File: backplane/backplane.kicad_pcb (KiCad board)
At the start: 2 copper layers, 150 x 150 mm, 14 parts

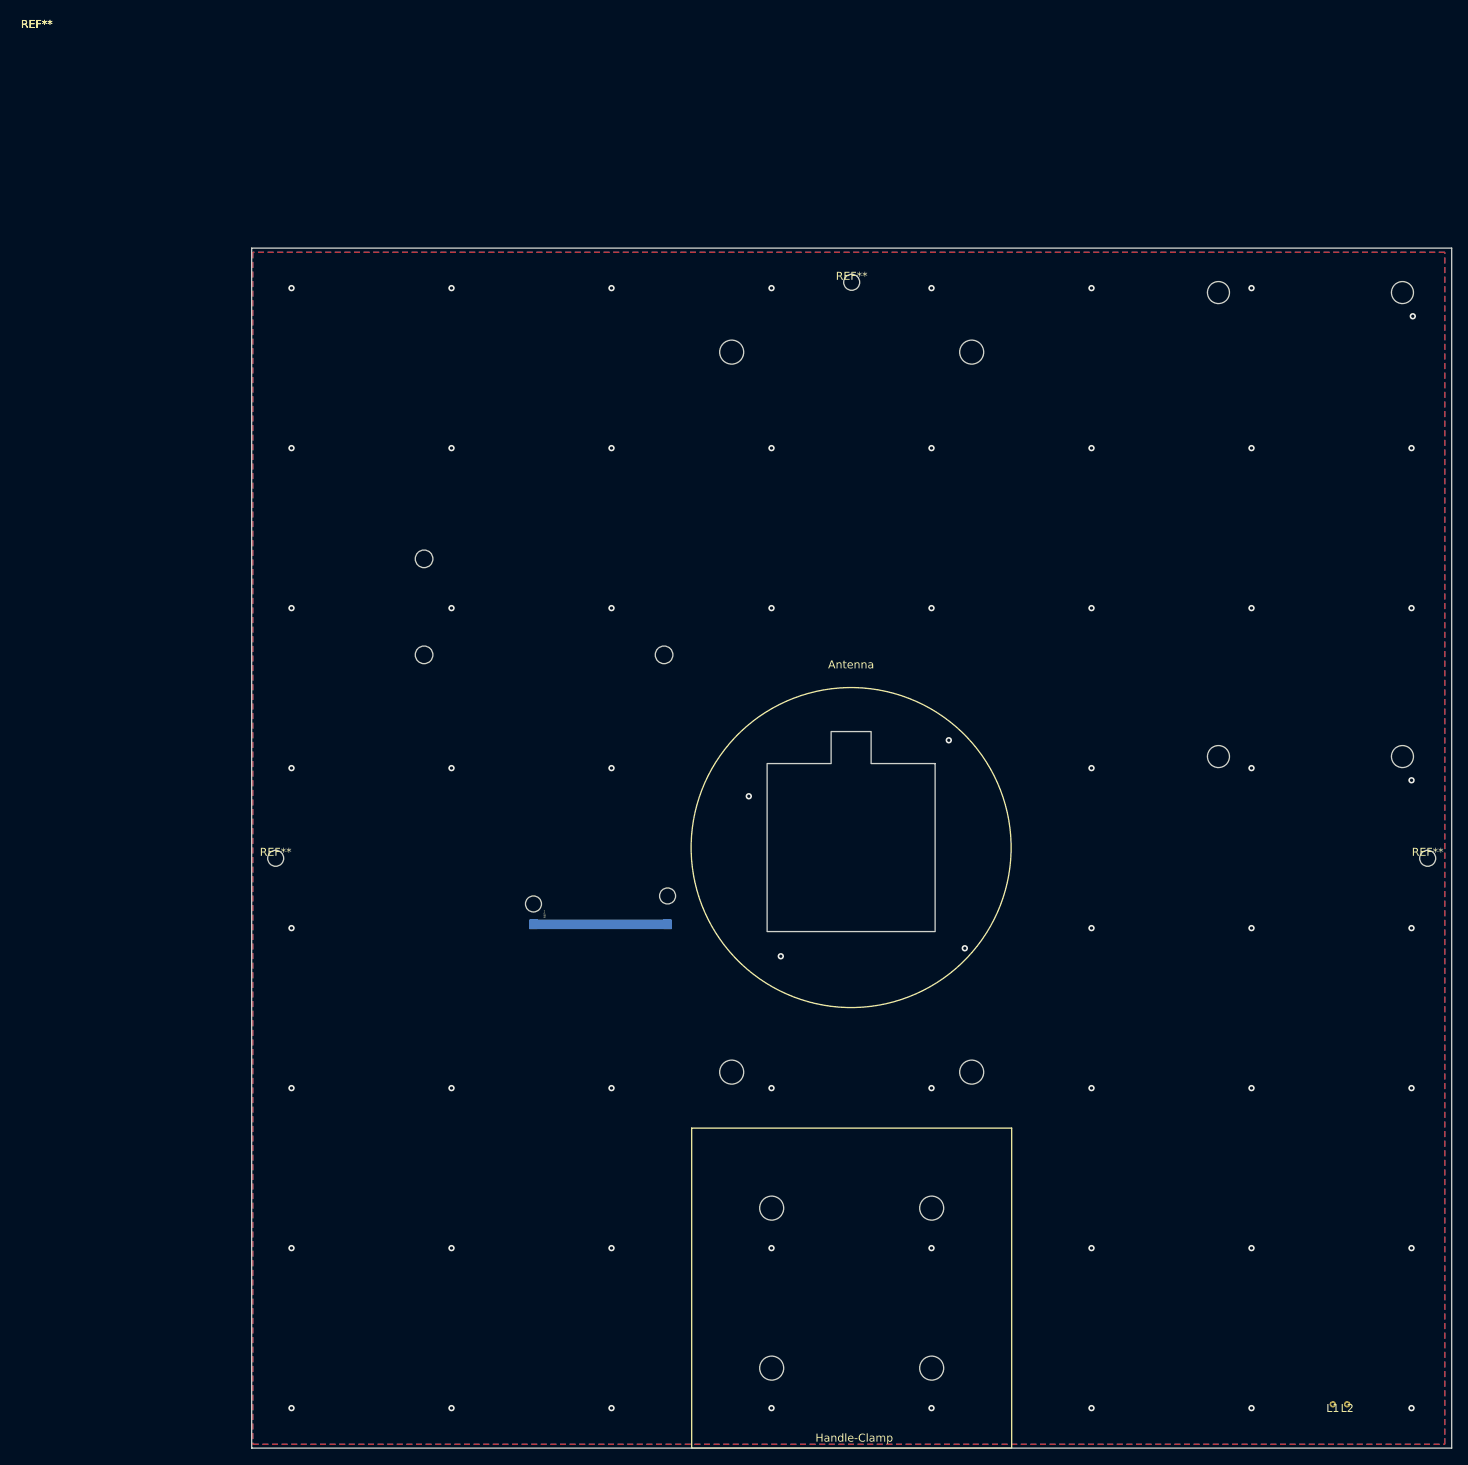
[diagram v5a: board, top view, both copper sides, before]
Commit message: Flipped layers for all components
The layer with silkscreen outlines for components is supposed to represent
what users should see when holding HGS.  This should be on the front layer
so that placement doesn't get flipped when it's on the back.
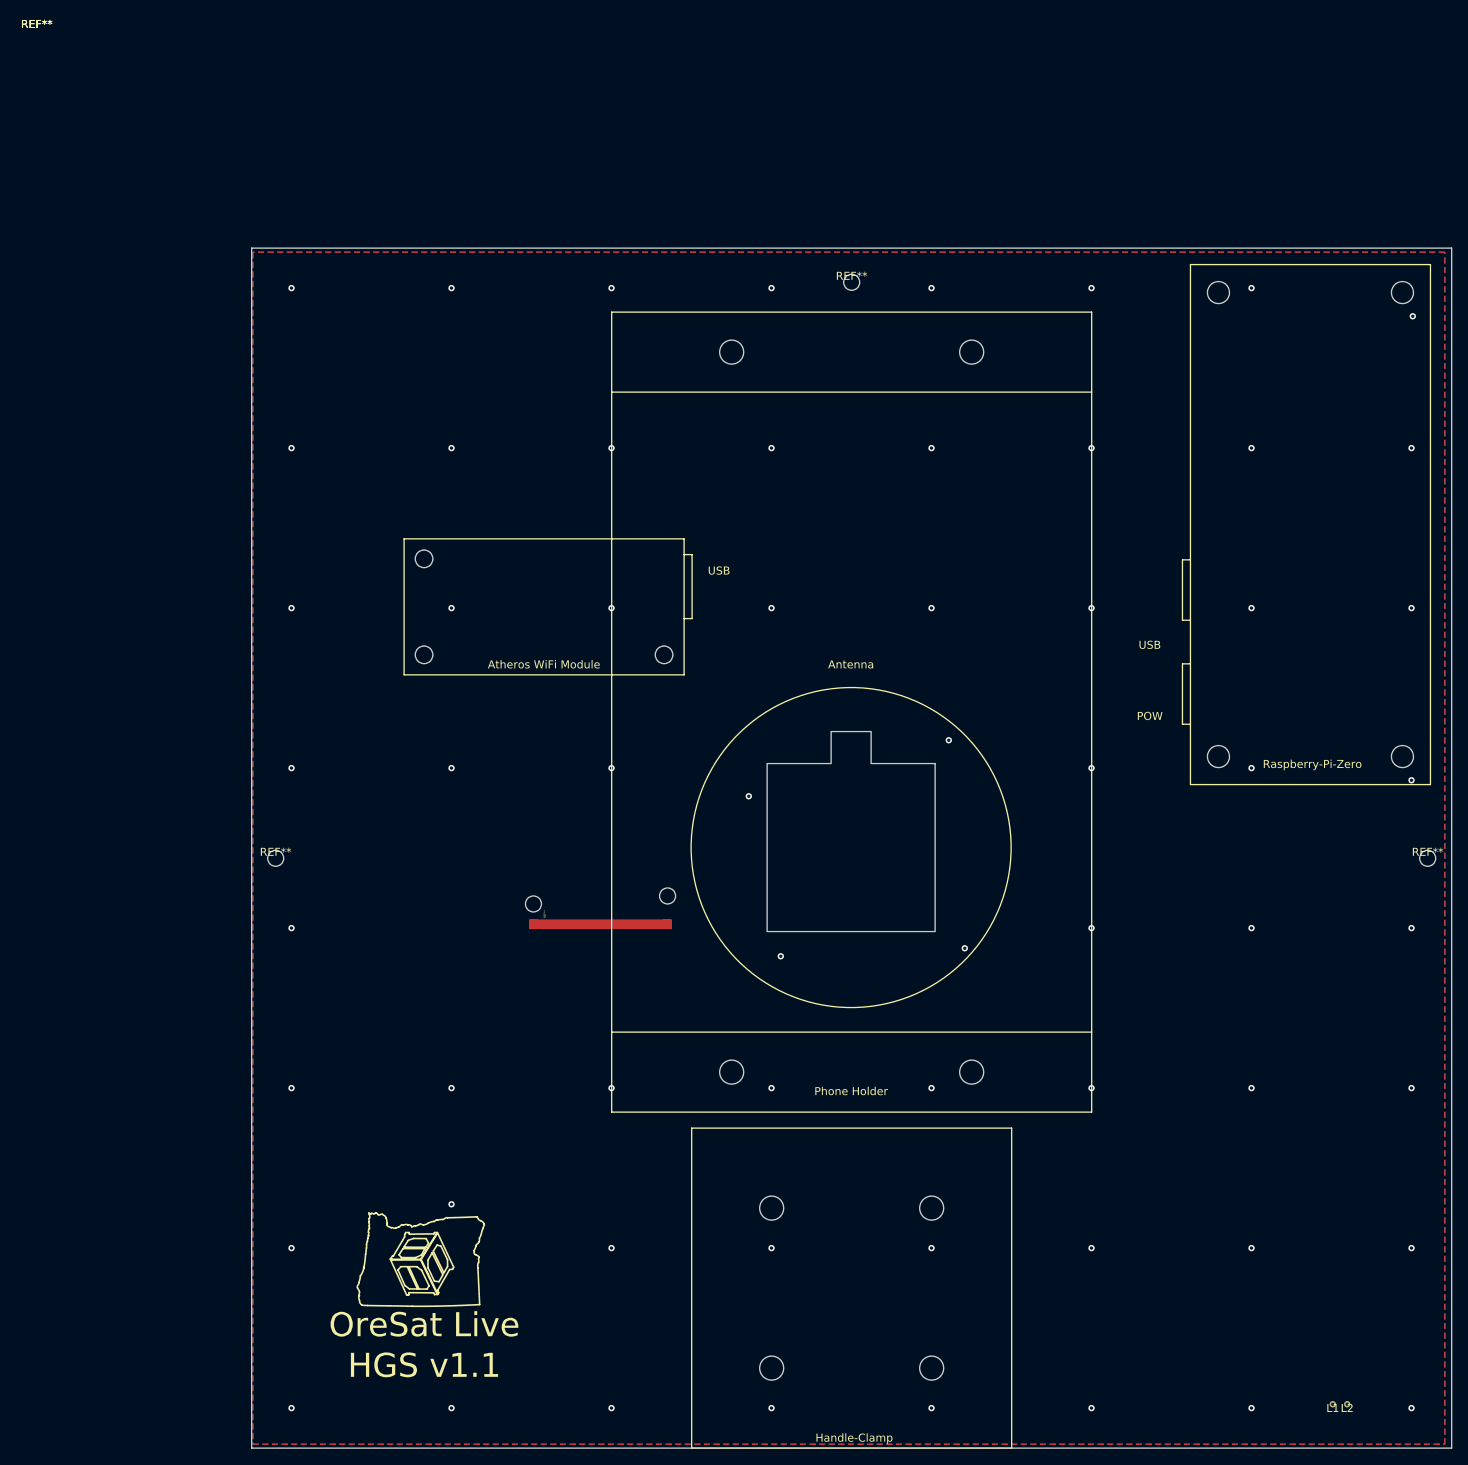
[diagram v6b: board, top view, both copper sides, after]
